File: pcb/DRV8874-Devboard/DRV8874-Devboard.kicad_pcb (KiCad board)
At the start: 4 copper layers, 65 x 67 mm, 61 parts, among them J1 Conn_01x04_Pin, J10 Conn_01x06_Pin, J12 Conn_01x03_Pin, J2 Screw_Terminal_01x02, J3 Conn_01x03_Pin, J4 Conn_01x03_Pin, J5 Conn_01x04_Pin, J6 Conn_01x03_Pin, J7 Conn_01x03_Pin, J8 Conn_01x03_Pin, J9 Conn_01x03_Pin, U1 DRV8874, U2 BL9342, U3 DRV8874, U4 SN65HVD230, U5 TPS16630PWPR, U6 M95320-WMN6TP, U7 TinyThinker_J1

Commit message: checkpoint
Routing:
- net /SPI2_MOSI: track 46.9 -> 55.6 mm
- net /SPI2_SCK: track 45.2 -> 53.9 mm
- net /SPI2_MISO: track 50.1 -> 57.4 mm
- net /SPI2_NSS: track 49.0 -> 55.9 mm
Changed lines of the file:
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@@
 	)
 	(via
-		(at 139.75 100.95)
+		(at 138 101.8)
 		(size 0.7)
 		(drill 0.3)
@@
 	)
 	(via
-		(at 140.25 96)
+		(at 138.5 95.6)
 		(size 0.7)
 		(drill 0.3)
@@
 	)
 	(via
-		(at 139.95 98.2)
+		(at 138.7 99.6)
 		(size 0.7)
 		(drill 0.3)
@@
 	)
 	(segment
+		(start 143.7 98.1)
+		(end 145.534999 98.1)
+		(width 0.3)
+		(layer "F.Cu")
+		(net 18)
+	)
+	(segment
+		(start 146.335 97.299999)
+		(end 146.335 96.425)
+		(width 0.3)
+		(layer "F.Cu")
+		(net 18)
+	)
+	(segment
+		(start 140.2 94.5)
+		(end 140.2 94.6)
+		(width 0.3)
+		(layer "F.Cu")
+		(net 18)
+	)
+	(segment
+		(start 140.2 94.6)
+		(end 143.7 98.1)
+		(width 0.3)
+		(layer "F.Cu")
+		(net 18)
+	)
+	(segment
+		(start 145.534999 98.1)
+		(end 146.335 97.299999)
+		(width 0.3)
+		(layer "F.Cu")
+		(net 18)
+	)
+	(segment
 		(start 99.6 92.1)
 		(end 99.6 92.5)
@@
 	)
 	(via
-		(at 140.185878 95.102284)
+		(at 140.2 94.5)
 		(size 0.7)
 		(drill 0.3)
@@
 	)
 	(segment
-		(start 140.185878 95.102284)
-		(end 137.583594 92.5)
+		(start 108 92.5)
+		(end 106.85 91.35)
+		(width 0.3)
+		(layer "B.Cu")
+		(net 18)
+	)
+	(segment
+		(start 106.85 91.35)
+		(end 100.05 91.35)
+		(width 0.3)
+		(layer "B.Cu")
+		(net 18)
+	)
+	(segment
+		(start 100.05 91.35)
+		(end 99.6 91.8)
 		(width 0.3)
 		(layer "B.Cu")
@@
 	)
 	(segment
-		(start 108 92.5)
-		(end 106.85 91.35)
+		(start 139.583594 94.5)
+		(end 137.583594 92.5)
 		(width 0.3)
 		(layer "B.Cu")
@@
 	)
 	(segment
-		(start 100.05 91.35)
-		(end 99.6 91.8)
-		(width 0.3)
-		(layer "B.Cu")
-		(net 18)
-	)
-	(segment
-		(start 106.85 91.35)
-		(end 100.05 91.35)
+		(start 140.2 94.5)
+		(end 139.583594 94.5)
 		(width 0.3)
 		(layer "B.Cu")
@@
 	)
 	(segment
-		(start 139.15 98.9)
-		(end 140.05 99.8)
+		(start 140.8 103.2)
+		(end 143.4 103.2)
 		(width 0.3)
 		(layer "F.Cu")
@@
 	)
 	(segment
-		(start 139 98.9)
-		(end 139.15 98.9)
+		(start 143.795 102.805)
+		(end 143.795 101.575)
+		(width 0.3)
+		(layer "F.Cu")
+		(net 26)
+	)
+	(segment
+		(start 138.4 100.8)
+		(end 140.8 103.2)
 		(width 0.3)
 		(layer "F.Cu")
@@
 	)
 	(segment
+		(start 143.4 103.2)
+		(end 143.795 102.805)
+		(width 0.3)
+		(layer "F.Cu")
+		(net 26)
+	)
+	(segment
 		(start 98.6 96.3)
 		(end 98.6 95.8)
@@
 	)
 	(via
-		(at 139 98.9)
-		(size 0.7)
-		(drill 0.3)
-		(layers "F.Cu" "B.Cu")
+		(at 138.4 100.8)
+		(size 0.7)
+		(drill 0.3)
+		(layers "F.Cu" "B.Cu")
+		(net 26)
+	)
+	(segment
+		(start 98.6 98.5)
+		(end 98.6 96.3)
+		(width 0.3)
+		(layer "B.Cu")
+		(net 26)
+	)
+	(segment
+		(start 138.4 100.8)
+		(end 136.1 98.5)
+		(width 0.3)
+		(layer "B.Cu")
+		(net 26)
+	)
+	(segment
+		(start 136.1 98.5)
+		(end 108.3 98.5)
+		(width 0.3)
+		(layer "B.Cu")
+		(net 26)
+	)
+	(segment
+		(start 108.3 98.5)
+		(end 106.8 100)
+		(width 0.3)
+		(layer "B.Cu")
+		(net 26)
+	)
+	(segment
+		(start 100.1 100)
+		(end 98.6 98.5)
+		(width 0.3)
+		(layer "B.Cu")
 		(net 26)
 	)
@@
 	)
 	(segment
-		(start 139 98.9)
-		(end 107.9 98.9)
-		(width 0.3)
-		(layer "B.Cu")
-		(net 26)
-	)
-	(segment
-		(start 100.1 100)
-		(end 98.6 98.5)
-		(width 0.3)
-		(layer "B.Cu")
-		(net 26)
-	)
-	(segment
-		(start 107.9 98.9)
-		(end 106.8 100)
-		(width 0.3)
-		(layer "B.Cu")
-		(net 26)
-	)
-	(segment
-		(start 98.6 98.5)
-		(end 98.6 96.3)
-		(width 0.3)
-		(layer "B.Cu")
-		(net 26)
-	)
-	(segment
-		(start 139 97.6)
-		(end 139.55 97.05)
+		(start 145.065 100.915)
+		(end 145.065 101.575)
 		(width 0.3)
 		(layer "F.Cu")
@@
 	)
 	(segment
+		(start 141.75 97.6)
+		(end 145.065 100.915)
+		(width 0.3)
+		(layer "F.Cu")
+		(net 27)
+	)
+	(segment
 		(start 98.81 90.09)
 		(end 101.73 90.09)
@@
 		(net 27)
 	)
+	(segment
+		(start 138.8 97.6)
+		(end 141.75 97.6)
+		(width 0.3)
+		(layer "F.Cu")
+		(net 27)
+	)
 	(via
 		(at 98 92.1)
@@
 	)
 	(via
-		(at 139 97.6)
-		(size 0.7)
-		(drill 0.3)
-		(layers "F.Cu" "B.Cu")
+		(at 138.8 97.6)
+		(size 0.7)
+		(drill 0.3)
+		(layers "F.Cu" "B.Cu")
+		(net 27)
+	)
+	(segment
+		(start 138.8 97.6)
+		(end 136.41005 97.6)
+		(width 0.3)
+		(layer "B.Cu")
+		(net 27)
+	)
+	(segment
+		(start 133.21005 94.4)
+		(end 110.85 94.4)
+		(width 0.3)
+		(layer "B.Cu")
+		(net 27)
+	)
+	(segment
+		(start 98 93.4)
+		(end 98 92.1)
+		(width 0.3)
+		(layer "B.Cu")
+		(net 27)
+	)
+	(segment
+		(start 98.45 93.85)
+		(end 98 93.4)
+		(width 0.3)
+		(layer "B.Cu")
+		(net 27)
+	)
+	(segment
+		(start 110.3 93.85)
+		(end 98.45 93.85)
+		(width 0.3)
+		(layer "B.Cu")
 		(net 27)
 	)
@@
 	)
 	(segment
-		(start 98.45 93.85)
-		(end 98 93.4)
-		(width 0.3)
-		(layer "B.Cu")
-		(net 27)
-	)
-	(segment
-		(start 139 97.6)
-		(end 136.41005 97.6)
-		(width 0.3)
-		(layer "B.Cu")
-		(net 27)
-	)
-	(segment
 		(start 110.85 94.4)
 		(end 110.3 93.85)
-		(width 0.3)
-		(layer "B.Cu")
-		(net 27)
-	)
-	(segment
-		(start 110.3 93.85)
-		(end 98.45 93.85)
-		(width 0.3)
-		(layer "B.Cu")
-		(net 27)
-	)
-	(segment
-		(start 133.21005 94.4)
-		(end 110.85 94.4)
-		(width 0.3)
-		(layer "B.Cu")
-		(net 27)
-	)
-	(segment
-		(start 98 93.4)
-		(end 98 92.1)
 		(width 0.3)
 		(layer "B.Cu")
@@
 	)
 	(segment
+		(start 140.2 92.9)
+		(end 140.3 92.8)
+		(width 0.3)
+		(layer "F.Cu")
+		(net 38)
+	)
+	(segment
+		(start 147.605 94.305)
+		(end 147.605 96.425)
+		(width 0.3)
+		(layer "F.Cu")
+		(net 38)
+	)
+	(segment
+		(start 146.1 92.8)
+		(end 147.605 94.305)
+		(width 0.3)
+		(layer "F.Cu")
+		(net 38)
+	)
+	(segment
 		(start 99.95 87.55)
 		(end 101.73 87.55)
@@
 	)
 	(segment
+		(start 140.3 92.8)
+		(end 146.1 92.8)
+		(width 0.3)
+		(layer "F.Cu")
+		(net 38)
+	)
+	(segment
 		(start 99.5 88.4)
 		(end 99.5 88)
@@
 	)
 	(via
-		(at 140.999997 94.5)
+		(at 140.2 92.9)
 		(size 0.7)
 		(drill 0.3)
@@
 	)
 	(segment
+		(start 99.5 88.5)
+		(end 99.5 88.4)
+		(width 0.3)
+		(layer "B.Cu")
+		(net 38)
+	)
+	(segment
+		(start 139.399997 92.9)
+		(end 137.599997 91.1)
+		(width 0.3)
+		(layer "B.Cu")
+		(net 38)
+	)
+	(segment
 		(start 99.8 88.8)
 		(end 99.5 88.5)
@@
 	)
 	(segment
-		(start 140.999997 94.5)
-		(end 137.599997 91.1)
+		(start 140.2 92.9)
+		(end 139.399997 92.9)
 		(width 0.3)
 		(layer "B.Cu")
@@
 	)
 	(segment
-		(start 99.5 88.5)
-		(end 99.5 88.4)
+		(start 117.25 91.1)
+		(end 115.85 89.7)
 		(width 0.3)
 		(layer "B.Cu")
@@
 		(width 0.3)
 		(layer "B.Cu")
-		(net 38)
-	)
-	(segment
-		(start 117.25 91.1)
-		(end 115.85 89.7)
-		(width 0.3)
-		(layer "B.Cu")

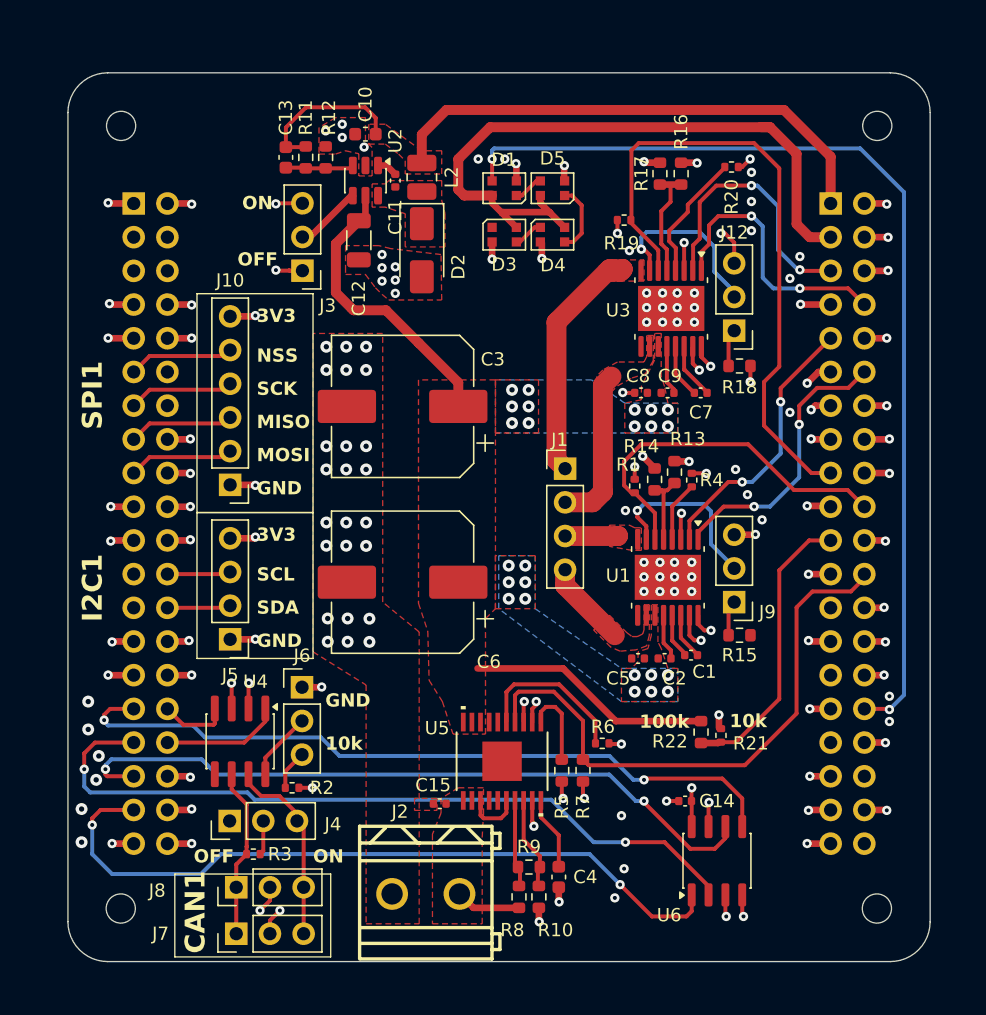
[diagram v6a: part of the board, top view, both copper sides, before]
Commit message: added connector for SWD
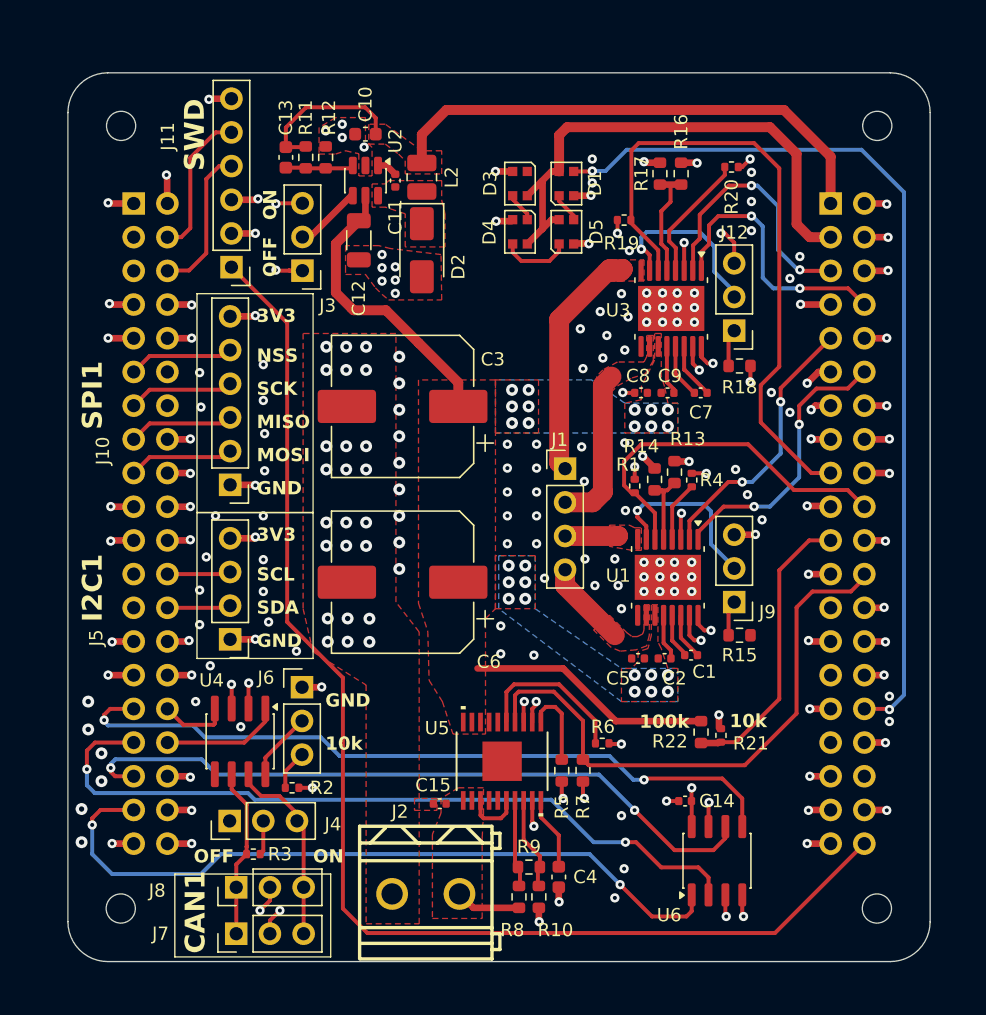
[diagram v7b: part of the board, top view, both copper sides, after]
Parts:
- added J11: Conn_01x06_Pin, Connector_PinHeader_2.54mm:PinHeader_1x06_P2.54mm_Vertical, F.Cu at (109.1, 54.2)
- moved D1 4.70 mm to (134.3, 48.0), turned to 90 degrees
- moved D3 4.03 mm to (130.8, 48.0), turned to -90 degrees
- moved D5 3.45 mm to (134.3, 51.6), turned to 90 degrees
- moved D4 2.46 mm to (130.8, 51.6), turned to -90 degrees
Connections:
- U7 pad 40: unconnected-(U7A-NRST-Pad40) -> /NRST
- U7 pad 44: unconnected-(U7B-SWDIO-Pad44) -> /SWDIO
- U7 pad 46: unconnected-(U7B-SWCLK-Pad46) -> /SWCLK
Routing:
- net /NRST: track 0.00 -> 94.7 mm
- net /SWCLK: track 0.00 -> 11.4 mm
- net +5V_SYS: track 51.3 -> 40.0 mm
- net /SWDIO: track 0.00 -> 11.2 mm
- net /RGB_LED_PWM: track 76.1 -> 68.3 mm
- net +3.3V: track 54.2 -> 57.6 mm, vias 31 -> 33
- net GND: track 99.0 -> 101.1 mm, vias 143 -> 202
- net /SPI2_SCK: track 53.9 -> 53.0 mm
- net /B_IN2: track 20.4 -> 19.8 mm
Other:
- board text added: "G"
- board text added: "N"
- board text added: "SWCLK"
- board text added: "SWD"
- board text added: "SWDIO"
- board text added: "V"

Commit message: added logo
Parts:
- added G***: LOGO, LOGO, B.Cu at (127.3, 85.8)
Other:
- board text added: "+ -"
- board text added: "09/2026 V1.0.0"
- board text added: "6-36V"
- board text added: "PSD-17 DevBoard"
- board text added: "Polar Robotics"
